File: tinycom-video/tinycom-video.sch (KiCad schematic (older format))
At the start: 42 parts, among them J1 MICRO_SD_HINGE, P1 CONN_02X10, P2 CONN_02X10, P4 USB_OTG, U1 SY8008BAAC, U2 AXP209, U3 SY8008BAAC, U4 RTL8188, U5 rainsun-antenna

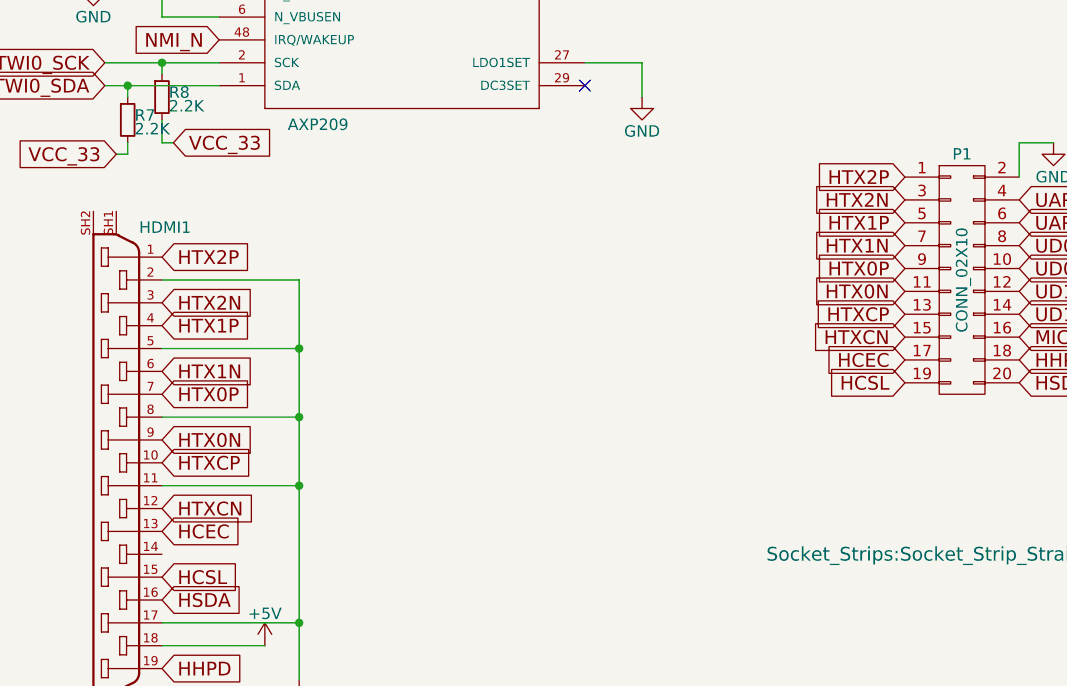
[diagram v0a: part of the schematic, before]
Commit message: move hdmi
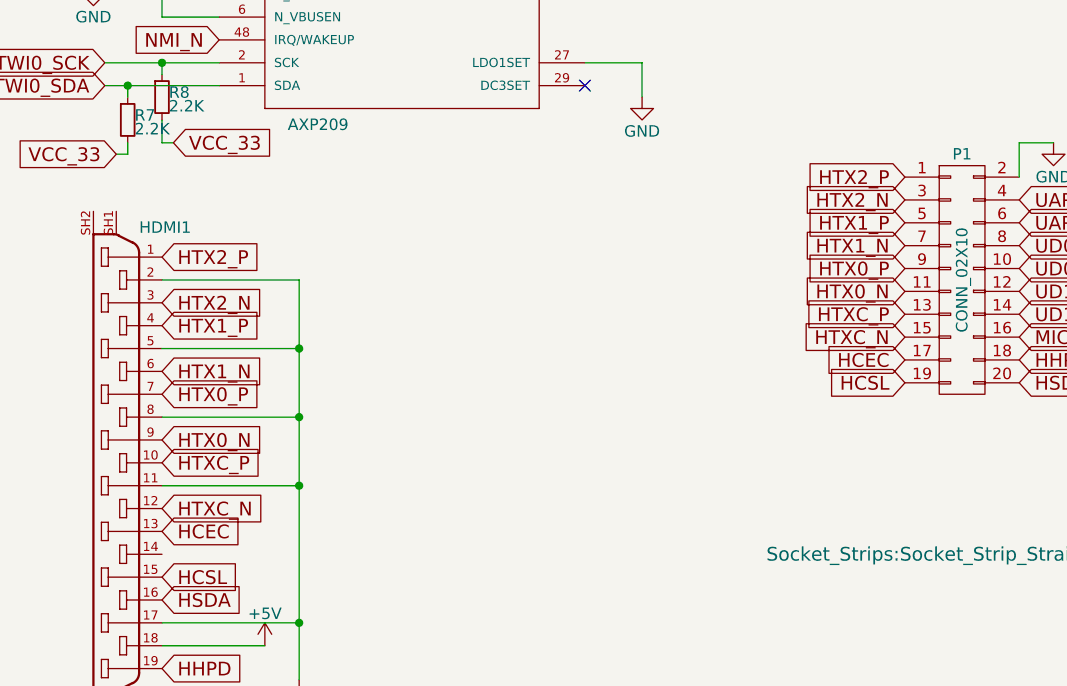
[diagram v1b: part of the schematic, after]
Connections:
- net HTX0N renamed HTX0_N
- net HTX0P renamed HTX0_P
- net HTX1N renamed HTX1_N
- net HTX1P renamed HTX1_P
- net HTX2N renamed HTX2_N
- net HTX2P renamed HTX2_P
- net HTXCN renamed HTXC_N
- net HTXCP renamed HTXC_P
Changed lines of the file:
@@
 $EndComp
 Text GLabel 4400 6150 0    60   Input ~ 0
-HTX2P
+HTX2_P
 Text GLabel 4400 6250 0    60   Input ~ 0
-HTX2N
+HTX2_N
 Text GLabel 4400 6350 0    60   Input ~ 0
-HTX1P
+HTX1_P
 Text GLabel 4400 6450 0    60   Input ~ 0
-HTX1N
+HTX1_N
 Text GLabel 4400 6550 0    60   Input ~ 0
-HTX0P
+HTX0_P
 Text GLabel 4400 6650 0    60   Input ~ 0
-HTX0N
+HTX0_N
 Text GLabel 4400 6750 0    60   Input ~ 0
-HTXCP
+HTXC_P
 Text GLabel 4400 6850 0    60   Input ~ 0
-HTXCN
+HTXC_N
 Text GLabel 4400 6950 0    60   Input ~ 0
 HCEC
@@
 $EndComp
 Text GLabel 1150 6500 2    60   Input ~ 0
-HTX2P
+HTX2_P
 Text GLabel 1150 6700 2    60   Input ~ 0
-HTX2N
+HTX2_N
 Text GLabel 1150 6800 2    60   Input ~ 0
-HTX1P
+HTX1_P
 Text GLabel 1150 7000 2    60   Input ~ 0
-HTX1N
+HTX1_N
 Text GLabel 1150 7100 2    60   Input ~ 0
-HTX0P
+HTX0_P
 Text GLabel 1150 7300 2    60   Input ~ 0
-HTX0N
+HTX0_N
 Text GLabel 1150 7600 2    60   Input ~ 0
-HTXCN
+HTXC_N
 Text GLabel 1150 7700 2    60   Input ~ 0
 HCEC
@@
 HHPD
 Text GLabel 1150 7400 2    60   Input ~ 0
-HTXCP
+HTXC_P
 $Comp
 L +5V #PWR035

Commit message: update base
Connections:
- net UART1_RX: now also P2.15 (P15); no longer P1.6 (P6)
- net UART1_TX: now also P2.17 (P17); no longer P1.4 (P4)
- net UD0_N: now also P1.6 (P6); no longer P1.10 (P10)
- net UD0_P: now also P1.4 (P4); no longer P1.8 (P8)
- net UD1_N: now also P1.10 (P10); no longer P1.14 (P14)
- net UD1_P: now also P1.8 (P8); no longer P1.12 (P12)
- net MICIN1: no longer names the net of P1.16 (P16)
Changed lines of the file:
@@
 	1    0    0    -1
 $EndComp
-Text GLabel 4900 6850 2    60   Input ~ 0
-MICIN1
-Text GLabel 4900 6650 2    60   Input ~ 0
+Text GLabel 4900 6450 2    60   Input ~ 0
 UD1_P
-Text GLabel 4900 6550 2    60   Input ~ 0
+Text GLabel 4900 6350 2    60   Input ~ 0
 UD0_N
 $Comp
@@
 Text GLabel 6600 6650 2    60   Input ~ 0
 SDC0_D1
-Text GLabel 4900 6350 2    60   Input ~ 0
+Text GLabel 6100 6950 0    60   Input ~ 0
 UART1_RX
-Text GLabel 4900 6450 2    60   Input ~ 0
+Text GLabel 4900 6250 2    60   Input ~ 0
 UD0_P
 $Comp
@@
 Text GLabel 6600 6250 2    60   Input ~ 0
 TWI0_SCK
-Text GLabel 4900 6250 2    60   Input ~ 0
+Text GLabel 6100 7050 0    60   Input ~ 0
 UART1_TX
 $Comp
@@
 	1    0    0    -1
 $EndComp
-Text GLabel 4900 6750 2    60   Input ~ 0
+Text GLabel 4900 6550 2    60   Input ~ 0
 UD1_N
 $Comp

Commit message: vid usb
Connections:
- net UD0_N: now also P4.2 (D-)
- net UD0_P: now also P4.3 (D+)
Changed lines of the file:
@@
 	1150 8100 1750 8100
 Connection ~ 1750 8100
+Text GLabel 5450 4450 0    60   Input ~ 0
+UD0_P
+Text GLabel 5450 4350 0    60   Input ~ 0
+UD0_N
 $EndSCHEMATC
